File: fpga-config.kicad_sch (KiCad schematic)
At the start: 34 parts, among them J1 PinHeader_2x7_P2mm_SMD_Shroud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, Q1 BSS138PW, Q2 BSS138PW, Q3 BSS138PW, SW1 CVS-03B, SW2 SW_KMR211NGLFS_SMD, U2 TPD4E05U06QDQARQ1, U30 REF3012AIDBZT, U34 XCAU25P-2FFVB676I, U35 TMP451AIDQFR

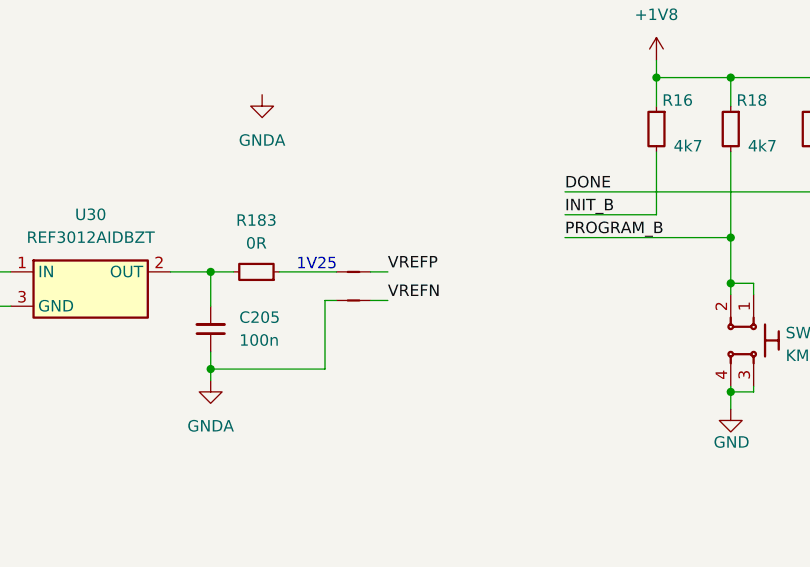
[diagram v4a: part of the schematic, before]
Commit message: [#66727] Update legacy footprints
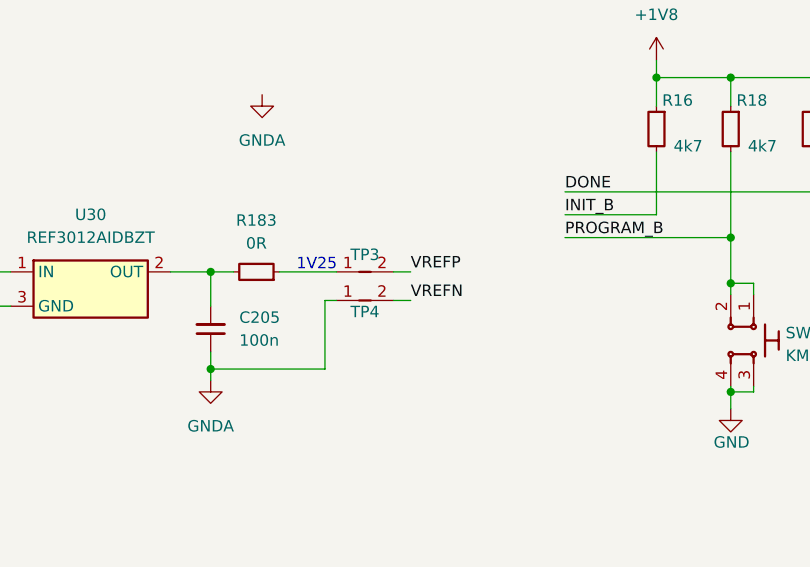
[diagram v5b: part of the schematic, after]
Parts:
- removed NT17, NT18: Net-Tie_2, K410T-devboard-footprints:NetTie-2_SMD_Pad0.127mm, symbol K410T-devboard:Net-Tie_2
- added TP3, TP4: Net-Tie_P0.127mm, antmicro-footprints:NetTie-2_SMD_Pad0.127mm, symbol ShuntsJumpers:Net-Tie_P0.127mm
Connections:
- net GNDA: now also TP4.1
- net VREFN: now also TP4.2
- net VREFP: now also TP3.2
- net at R183.1: now also TP3.1
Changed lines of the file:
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@@
     (stroke (width 0) (type default))
   )
-  (wire (pts (xy 139.065 86.995) (xy 140.97 86.995))
+  (wire (pts (xy 141.605 86.995) (xy 143.51 86.995))
     (stroke (width 0) (type default))
   )
@@
     (stroke (width 0) (type default))
   )
-  (wire (pts (xy 139.065 83.82) (xy 140.97 83.82))
+  (wire (pts (xy 141.605 83.82) (xy 143.51 83.82))
     (stroke (width 0) (type default))
   )
@@
     (effects (font (size 1.27 1.27)) (justify left bottom))
   )
-  (label "VREFN" (at 140.97 86.995 0) (fields_autoplaced)
+  (label "VREFN" (at 143.51 86.995 0) (fields_autoplaced)
     (effects (font (size 1.27 1.27)) (justify left bottom))
   )
@@
     (effects (font (size 1.27 1.27)) (justify left bottom))
   )
-  (label "VREFP" (at 140.97 83.82 0) (fields_autoplaced)
+  (label "VREFP" (at 143.51 83.82 0) (fields_autoplaced)
     (effects (font (size 1.27 1.27)) (justify left bottom))
   )
@@
     )
   )
-  (symbol (lib_id "K410T-devboard:Net-Tie_2") (at 135.255 83.82 0) (unit 1)
-    (in_bom yes) (on_board yes) (dnp no) (fields_autoplaced)
-    (property "Reference" "NT17" (at 135.255 82.55 0)
-      (effects (font (size 1.27 1.27)) hide)
-    )
-    (property "Value" "Net-Tie_2" (at 137.16 81.28 0)
-      (effects (font (size 1.27 1.27) (thickness 0.15)) hide)
-    )
-    (property "Footprint" "K410T-devboard-footprints:NetTie-2_SMD_Pad0.127mm" (at 156.845 88.9 0)
-      (effects (font (size 1.27 1.27) (thickness 0.15)) (justify left bottom) hide)
-    )
-    (property "Datasheet" "" (at 156.845 91.44 0)
-      (effects (font (size 1.27 1.27) (thickness 0.15)) (justify left bottom) hide)
-    )
-    (property "MPN" "" (at 156.845 92.71 0)
-      (effects (font (size 1.27 1.27)) (justify left) hide)
-    )
-    (property "Manufacturer" "" (at 156.845 95.25 0)
-      (effects (font (size 1.27 1.27)) (justify left) hide)
-    )
-    (property "Author" "Antmicro" (at 156.845 99.06 0)
-      (effects (font (size 1.27 1.27) (thickness 0.15)) (justify left bottom) hide)
-    )
-    (property "License" "Apache-2.0" (at 156.845 101.6 0)
-      (effects (font (size 1.27 1.27) (thickness 0.15)) (justify left bottom) hide)
-    )
-    (pin "1")
-    (pin "2")
-    (instances
-      (project "data-center-rdimm-ddr5-tester"
-        (path "/1faa6543-e26a-4449-8bac-ee14b9f19e5f/00000000-0000-0000-0000-00005fd53c7d"
-          (reference "NT17") (unit 1)
-        )
-      )
-    )
-  )
   (symbol (lib_id "antmicroResistors0402:R_100R_0402") (at 92.71 163.957 270) (unit 1)
     (in_bom no) (on_board yes) (dnp yes) (fields_autoplaced)
@@
     )
   )
-  (symbol (lib_id "K410T-devboard:Net-Tie_2") (at 135.255 86.995 0) (unit 1)
-    (in_bom yes) (on_board yes) (dnp no) (fields_autoplaced)
-    (property "Reference" "NT18" (at 135.255 85.725 0)
-      (effects (font (size 1.27 1.27)) hide)
-    )
-    (property "Value" "Net-Tie_2" (at 137.16 83.82 0)
-      (effects (font (size 1.27 1.27) (thickness 0.15)) hide)
-    )
-    (property "Footprint" "K410T-devboard-footprints:NetTie-2_SMD_Pad0.127mm" (at 156.845 92.075 0)
-      (effects (font (size 1.27 1.27) (thickness 0.15)) (justify left bottom) hide)
-    )
-    (property "Datasheet" "" (at 156.845 94.615 0)
-      (effects (font (size 1.27 1.27) (thickness 0.15)) (justify left bottom) hide)
-    )
-    (property "MPN" "" (at 156.845 95.885 0)
-      (effects (font (size 1.27 1.27)) (justify left) hide)
-    )
-    (property "Manufacturer" "" (at 156.845 98.425 0)
-      (effects (font (size 1.27 1.27)) (justify left) hide)
-    )
-    (property "Author" "Antmicro" (at 156.845 102.235 0)
-      (effects (font (size 1.27 1.27) (thickness 0.15)) (justify left bottom) hide)
-    )
-    (property "License" "Apache-2.0" (at 156.845 104.775 0)
-      (effects (font (size 1.27 1.27) (thickness 0.15)) (justify left bottom) hide)
-    )
-    (pin "1")
-    (pin "2")
-    (instances
-      (project "data-center-rdimm-ddr5-tester"
-        (path "/1faa6543-e26a-4449-8bac-ee14b9f19e5f/00000000-0000-0000-0000-00005fd53c7d"
-          (reference "NT18") (unit 1)
-        )
-      )
-    )
-  )
   (symbol (lib_id "antmicropower:+3V3") (at 164.465 226.06 0) (unit 1)
     (in_bom yes) (on_board yes) (dnp no) (fields_autoplaced)
@@
     )
   )
+  (symbol (lib_id "ShuntsJumpers:Net-Tie_P0.127mm") (at 135.255 86.995 0) (unit 1)
+    (in_bom no) (on_board yes) (dnp no)
+    (property "Reference" "TP4" (at 138.43 88.265 0)
+      (effects (font (size 1.27 1.27) (thickness 0.15)))
+    )
+    (property "Value" "Net-Tie_P0.127mm" (at 138.43 85.09 0)
+      (effects (font (size 1.27 1.27) (thickness 0.15)) hide)
+    )
+    (property "Footprint" "antmicro-footprints:NetTie-2_SMD_Pad0.127mm" (at 156.845 99.695 0)
+      (effects (font (size 1.27 1.27) (thickness 0.15)) (justify left bottom) hide)
+    )
+    (property "Datasheet" "" (at 156.845 102.235 0)
+      (effects (font (size 1.27 1.27) (thickness 0.15)) (justify left bottom) hide)
+    )
+    (property "MPN" "" (at 156.845 97.155 0)
+      (effects (font (size 1.27 1.27) (thickness 0.15)) (justify left bottom))
+    )
+    (property "Manufacturer" "" (at 156.845 104.775 0)
+      (effects (font (size 1.27 1.27) (thickness 0.15)) (justify left bottom) hide)
+    )
+    (property "Author" "Antmicro" (at 156.845 107.315 0)
+      (effects (font (size 1.27 1.27) (thickness 0.15)) (justify left bottom) hide)
+    )
+    (property "License" "Apache-2.0" (at 156.845 109.855 0)
+      (effects (font (size 1.27 1.27) (thickness 0.15)) (justify left bottom) hide)
+    )
+    (pin "2")
+    (pin "1")
+    (instances
+      (project "data-center-rdimm-ddr5-tester"
+        (path "/1faa6543-e26a-4449-8bac-ee14b9f19e5f/00000000-0000-0000-0000-00005fd53c7d"
+          (reference "TP4") (unit 1)
+        )
+      )
+    )
+  )
   (symbol (lib_id "antmicropower:GNDA") (at 127 64.135 0) (unit 1)
     (in_bom yes) (on_board yes) (dnp no) (fields_autoplaced)
@@
         )
       )
+    )
+  )
+  (symbol (lib_id "ShuntsJumpers:Net-Tie_P0.127mm") (at 135.255 83.82 0) (unit 1)
+    (in_bom no) (on_board yes) (dnp no)
+    (property "Reference" "TP3" (at 138.43 81.915 0)
+      (effects (font (size 1.27 1.27) (thickness 0.15)))
+    )
+    (property "Value" "Net-Tie_P0.127mm" (at 138.43 81.915 0)
+      (effects (font (size 1.27 1.27) (thickness 0.15)) hide)
+    )
+    (property "Footprint" "antmicro-footprints:NetTie-2_SMD_Pad0.127mm" (at 156.845 96.52 0)
+      (effects (font (size 1.27 1.27) (thickness 0.15)) (justify left bottom) hide)
+    )
+    (property "Datasheet" "" (at 156.845 99.06 0)
+      (effects (font (size 1.27 1.27) (thickness 0.15)) (justify left bottom) hide)
+    )
+    (property "MPN" "" (at 156.845 93.98 0)
+      (effects (font (size 1.27 1.27) (thickness 0.15)) (justify left bottom))
+    )
+    (property "Manufacturer" "" (at 156.845 101.6 0)
+      (effects (font (size 1.27 1.27) (thickness 0.15)) (justify left bottom) hide)
+    )
+    (property "Author" "Antmicro" (at 156.845 104.14 0)
+      (effects (font (size 1.27 1.27) (thickness 0.15)) (justify left bottom) hide)
+    )
+    (property "License" "Apache-2.0" (at 156.845 106.68 0)
+      (effects (font (size 1.27 1.27) (thickness 0.15)) (justify left bottom) hide)
+    )
+    (pin "2")
+    (pin "1")
+    (instances
+      (project "data-center-rdimm-ddr5-tester"
+        (path "/1faa6543-e26a-4449-8bac-ee14b9f19e5f/00000000-0000-0000-0000-00005fd53c7d"
+          (reference "TP3") (unit 1)
+        )
+      )
